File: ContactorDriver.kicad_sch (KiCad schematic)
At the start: 26 parts, among them Con1 LED, Con2 LED, J13 Conn_01x04, J14 Conn_01x04, Q2 IRLML0030, Q3 IRLML0030, U4 TCMT1106, U5 TCMT1106

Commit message: is it time to give up :3
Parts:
- renumbered C11 to C12, C12 to C13, C13 to C14, C14 to C15, D8 to D7, D9 to D8, J13 to J12, J14 to J13
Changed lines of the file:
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@@
 		(dnp no)
 		(fields_autoplaced yes)
-		(property "Reference" "#PWR053"
+		(property "Reference" "#PWR050"
 			(at 112.395 36.83 0)
 			(effects
@@
 			(project "VehicleControlUnit"
 				(path "/795c8e51-3ded-4d21-b864-aaff31c5def7/838dfc75-afcf-4845-8c43-fcef4e0ee00c"
-					(reference "#PWR053")
+					(reference "#PWR050")
 					(unit 1)
 				)
@@
 		(dnp no)
 		(fields_autoplaced yes)
-		(property "Reference" "C11"
+		(property "Reference" "C12"
 			(at 59.055 117.4749 0)
 			(effects
@@
 			(project ""
 				(path "/795c8e51-3ded-4d21-b864-aaff31c5def7/838dfc75-afcf-4845-8c43-fcef4e0ee00c"
-					(reference "C11")
+					(reference "C12")
 					(unit 1)
 				)
@@
 		(dnp no)
 		(fields_autoplaced yes)
-		(property "Reference" "C13"
+		(property "Reference" "C14"
 			(at 179.705 118.1099 0)
 			(effects
@@
 			(project "VehicleControlUnit"
 				(path "/795c8e51-3ded-4d21-b864-aaff31c5def7/838dfc75-afcf-4845-8c43-fcef4e0ee00c"
-					(reference "C13")
+					(reference "C14")
 					(unit 1)
 				)
@@
 		(dnp no)
 		(fields_autoplaced yes)
-		(property "Reference" "D8"
+		(property "Reference" "D7"
 			(at 114.935 43.8149 90)
 			(effects
@@
 			(project "VehicleControlUnit"
 				(path "/795c8e51-3ded-4d21-b864-aaff31c5def7/838dfc75-afcf-4845-8c43-fcef4e0ee00c"
-					(reference "D8")
+					(reference "D7")
 					(unit 1)
 				)
@@
 		(dnp no)
 		(fields_autoplaced yes)
-		(property "Reference" "#PWR054"
+		(property "Reference" "#PWR051"
 			(at 226.695 105.41 0)
 			(effects
@@
 			(project "VehicleControlUnit"
 				(path "/795c8e51-3ded-4d21-b864-aaff31c5def7/838dfc75-afcf-4845-8c43-fcef4e0ee00c"
-					(reference "#PWR054")
+					(reference "#PWR051")
 					(unit 1)
 				)
@@
 		(on_board yes)
 		(dnp no)
-		(property "Reference" "C12"
+		(property "Reference" "C13"
 			(at 100.965 112.3949 0)
 			(effects
@@
 			(project "VehicleControlUnit"
 				(path "/795c8e51-3ded-4d21-b864-aaff31c5def7/838dfc75-afcf-4845-8c43-fcef4e0ee00c"
-					(reference "C12")
+					(reference "C13")
 					(unit 1)
 				)
@@
 		(dnp no)
 		(fields_autoplaced yes)
-		(property "Reference" "#PWR055"
+		(property "Reference" "#PWR052"
 			(at 234.315 38.1 0)
 			(effects
@@
 			(project "VehicleControlUnit"
 				(path "/795c8e51-3ded-4d21-b864-aaff31c5def7/838dfc75-afcf-4845-8c43-fcef4e0ee00c"
-					(reference "#PWR055")
+					(reference "#PWR052")
 					(unit 1)
 				)
@@
 		(on_board yes)
 		(dnp no)
-		(property "Reference" "C14"
+		(property "Reference" "C15"
 			(at 222.885 113.0299 0)
 			(effects
@@
 			(project "VehicleControlUnit"
 				(path "/795c8e51-3ded-4d21-b864-aaff31c5def7/838dfc75-afcf-4845-8c43-fcef4e0ee00c"
-					(reference "C14")
+					(reference "C15")
 					(unit 1)
 				)
@@
 		(dnp no)
 		(fields_autoplaced yes)
-		(property "Reference" "#PWR052"
+		(property "Reference" "#PWR049"
 			(at 106.045 104.775 0)
 			(effects
@@
 			(project "VehicleControlUnit"
 				(path "/795c8e51-3ded-4d21-b864-aaff31c5def7/838dfc75-afcf-4845-8c43-fcef4e0ee00c"
-					(reference "#PWR052")
+					(reference "#PWR049")
 					(unit 1)
 				)
@@
 		(on_board yes)
 		(dnp no)
-		(property "Reference" "J14"
+		(property "Reference" "J13"
 			(at 245.745 106.6801 0)
 			(effects
@@
 			(project "VehicleControlUnit"
 				(path "/795c8e51-3ded-4d21-b864-aaff31c5def7/838dfc75-afcf-4845-8c43-fcef4e0ee00c"
-					(reference "J14")
+					(reference "J13")
 					(unit 1)
 				)
@@
 		(on_board yes)
 		(dnp no)
-		(property "Reference" "J13"
+		(property "Reference" "J12"
 			(at 123.825 106.0451 0)
 			(effects
@@
 			(project "VehicleControlUnit"
 				(path "/795c8e51-3ded-4d21-b864-aaff31c5def7/838dfc75-afcf-4845-8c43-fcef4e0ee00c"
-					(reference "J13")
+					(reference "J12")
 					(unit 1)
 				)
@@
 		(dnp no)
 		(fields_autoplaced yes)
-		(property "Reference" "D9"
+		(property "Reference" "D8"
 			(at 236.855 44.4499 90)
 			(effects
@@
 			(project "VehicleControlUnit"
 				(path "/795c8e51-3ded-4d21-b864-aaff31c5def7/838dfc75-afcf-4845-8c43-fcef4e0ee00c"
-					(reference "D9")
-					(unit 1)
-				)
+					(reference "D8")
+					(unit 1)
+				)

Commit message: 24v changes
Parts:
- R17, R19, R22, R24: value 2k -> 4k
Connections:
- net +12V renamed +24V
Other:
- note added: "MPre_Sense+"
- note added: "M_Sense+"

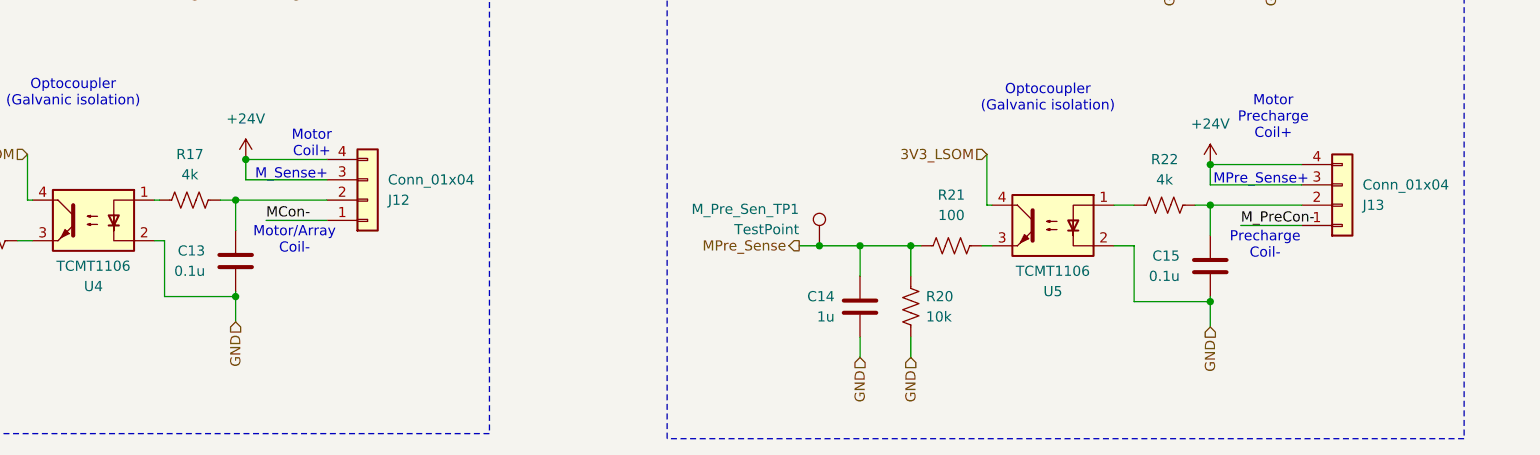
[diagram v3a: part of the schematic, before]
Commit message: moving to kicad-bild
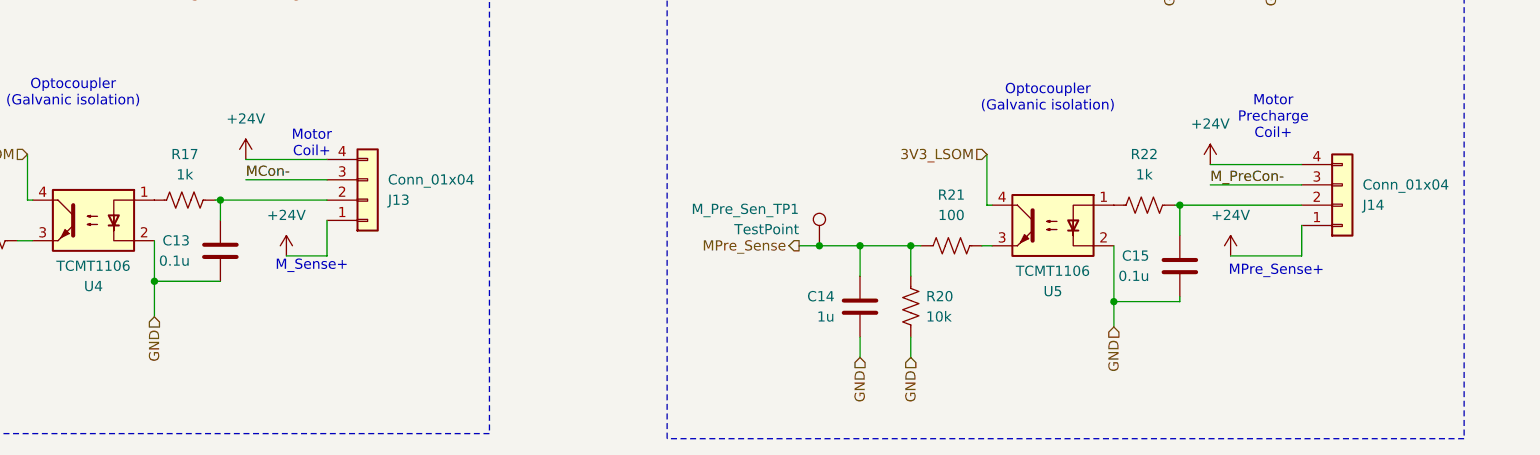
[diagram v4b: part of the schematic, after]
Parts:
- R17, R22: value 4k -> 1k
- renumbered J12 to J13, J13 to J14
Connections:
- net +24V: now also J13.1 (Pin_1), J14.1 (Pin_1); no longer J13.3 (Pin_3), J14.3 (Pin_3)
- net MCon-: now also J13.3 (Pin_3); no longer J13.1 (Pin_1)
- net M_PreCon-: now also J14.3 (Pin_3); no longer J14.1 (Pin_1)
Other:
- note removed: "Motor/Array Coil-"
- note removed: "Precharge Coil-"
- moved on the sheet: C13, C15, R17, R22

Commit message: fuck the rats nest im doing it tomorrow
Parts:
- D7, D8: footprint Active-PrechargeLib:SODFL4724X108N -> UTSVT_Passives:SODFL4724X108N
- J10: renamed from J13; footprint utsvt_conn:Molex_MicroFit3.0_1x4xP3.00mm_PolarizingPeg_Vertical -> UTSVT_Connectors:Molex_MicroFit3.0_1x4xP3.00mm_PolarizingPeg_Vertical
- J11: renamed from J14; footprint utsvt_conn:Molex_MicroFit3.0_1x4xP3.00mm_PolarizingPeg_Vertical -> UTSVT_Connectors:Molex_MicroFit3.0_1x4xP3.00mm_PolarizingPeg_Vertical
- renumbered C12 to C13, C13 to C14, C14 to C15, C15 to C16, R15 to R12, R16 to R13, R17 to R14, R18 to R15, R19 to R16, R20 to R17, R21 to R18, R22 to R19, R23 to R20, R24 to R21, U4 to U5, U5 to U6
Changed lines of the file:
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@@
 		(dnp no)
 		(fields_autoplaced yes)
-		(property "Reference" "R17"
+		(property "Reference" "R14"
 			(at 98.425 100.33 90)
 			(effects
@@
 			(project "VehicleControlUnit"
 				(path "/795c8e51-3ded-4d21-b864-aaff31c5def7/838dfc75-afcf-4845-8c43-fcef4e0ee00c"
-					(reference "R17")
+					(reference "R14")
 					(unit 1)
 				)
@@
 		(dnp no)
 		(fields_autoplaced yes)
-		(property "Reference" "#PWR054"
+		(property "Reference" "#PWR055"
 			(at 226.695 105.41 0)
 			(effects
@@
 			(project "VehicleControlUnit"
 				(path "/795c8e51-3ded-4d21-b864-aaff31c5def7/838dfc75-afcf-4845-8c43-fcef4e0ee00c"
-					(reference "#PWR054")
+					(reference "#PWR055")
 					(unit 1)
 				)
@@
 		(dnp no)
 		(fields_autoplaced yes)
-		(property "Reference" "R15"
+		(property "Reference" "R12"
 			(at 70.485 117.4749 0)
 			(effects
@@
 			(project ""
 				(path "/795c8e51-3ded-4d21-b864-aaff31c5def7/838dfc75-afcf-4845-8c43-fcef4e0ee00c"
-					(reference "R15")
+					(reference "R12")
 					(unit 1)
 				)
@@
 		(on_board yes)
 		(dnp no)
-		(property "Reference" "R18"
+		(property "Reference" "R15"
 			(at 102.235 69.2149 0)
 			(effects
@@
 			(project "VehicleControlUnit"
 				(path "/795c8e51-3ded-4d21-b864-aaff31c5def7/838dfc75-afcf-4845-8c43-fcef4e0ee00c"
-					(reference "R18")
+					(reference "R15")
 					(unit 1)
 				)
@@
 		(dnp no)
 		(fields_autoplaced yes)
-		(property "Reference" "U5"
+		(property "Reference" "U6"
 			(at 207.01 117.475 0)
 			(effects
@@
 			(project "VehicleControlUnit"
 				(path "/795c8e51-3ded-4d21-b864-aaff31c5def7/838dfc75-afcf-4845-8c43-fcef4e0ee00c"
-					(reference "U5")
+					(reference "U6")
 					(unit 1)
 				)
@@
 		(dnp no)
 		(fields_autoplaced yes)
-		(property "Reference" "C12"
+		(property "Reference" "C13"
 			(at 59.055 117.4749 0)
 			(effects
@@
 			(project ""
 				(path "/795c8e51-3ded-4d21-b864-aaff31c5def7/838dfc75-afcf-4845-8c43-fcef4e0ee00c"
-					(reference "C12")
+					(reference "C13")
 					(unit 1)
 				)
@@
 		(dnp no)
 		(fields_autoplaced yes)
-		(property "Reference" "R24"
+		(property "Reference" "R21"
 			(at 225.425 33.02 90)
 			(effects
@@
 			(project "VehicleControlUnit"
 				(path "/795c8e51-3ded-4d21-b864-aaff31c5def7/838dfc75-afcf-4845-8c43-fcef4e0ee00c"
-					(reference "R24")
+					(reference "R21")
 					(unit 1)
 				)
@@
 		(dnp no)
 		(fields_autoplaced yes)
-		(property "Reference" "R20"
+		(property "Reference" "R17"
 			(at 191.135 118.1099 0)
 			(effects
@@
 			(project "VehicleControlUnit"
 				(path "/795c8e51-3ded-4d21-b864-aaff31c5def7/838dfc75-afcf-4845-8c43-fcef4e0ee00c"
-					(reference "R20")
+					(reference "R17")
 					(unit 1)
 				)
@@
 		(dnp no)
 		(fields_autoplaced yes)
-		(property "Reference" "C14"
+		(property "Reference" "C15"
 			(at 179.705 118.1099 0)
 			(effects
@@
 			(project "VehicleControlUnit"
 				(path "/795c8e51-3ded-4d21-b864-aaff31c5def7/838dfc75-afcf-4845-8c43-fcef4e0ee00c"
-					(reference "C14")
+					(reference "C15")
 					(unit 1)
 				)
@@
 			)
 		)
-		(property "Footprint" "Active-PrechargeLib:SODFL4724X108N"
+		(property "Footprint" "UTSVT_Passives:SODFL4724X108N"
 			(at 112.395 45.085 0)
 			(effects
@@
 		(dnp no)
 		(fields_autoplaced yes)
-		(property "Reference" "R22"
+		(property "Reference" "R19"
 			(at 218.44 100.33 90)
 			(effects
@@
 			(project "VehicleControlUnit"
 				(path "/795c8e51-3ded-4d21-b864-aaff31c5def7/838dfc75-afcf-4845-8c43-fcef4e0ee00c"
-					(reference "R22")
+					(reference "R19")
 					(unit 1)
 				)
@@
 		(dnp no)
 		(fields_autoplaced yes)
-		(property "Reference" "#PWR053"
+		(property "Reference" "#PWR054"
 			(at 112.395 36.83 0)
 			(effects
@@
 			(project "VehicleControlUnit"
 				(path "/795c8e51-3ded-4d21-b864-aaff31c5def7/838dfc75-afcf-4845-8c43-fcef4e0ee00c"
-					(reference "#PWR053")
+					(reference "#PWR054")
 					(unit 1)
 				)
@@
 		(dnp no)
 		(fields_autoplaced yes)
-		(property "Reference" "#PWR051"
+		(property "Reference" "#PWR052"
 			(at 106.045 104.775 0)
 			(effects
@@
 			(project "VehicleControlUnit"
 				(path "/795c8e51-3ded-4d21-b864-aaff31c5def7/838dfc75-afcf-4845-8c43-fcef4e0ee00c"
-					(reference "#PWR051")
+					(reference "#PWR052")
 					(unit 1)
 				)
@@
 		(on_board yes)
 		(dnp no)
-		(property "Reference" "C13"
+		(property "Reference" "C14"
 			(at 99.06 111.1249 0)
 			(effects
@@
 			(project "VehicleControlUnit"
 				(path "/795c8e51-3ded-4d21-b864-aaff31c5def7/838dfc75-afcf-4845-8c43-fcef4e0ee00c"
-					(reference "C13")
+					(reference "C14")
 					(unit 1)
 				)
@@
 		(dnp no)
 		(fields_autoplaced yes)
-		(property "Reference" "#PWR052"
+		(property "Reference" "#PWR053"
 			(at 111.125 116.84 0)
 			(effects
@@
 			(project "VehicleControlUnit"
 				(path "/795c8e51-3ded-4d21-b864-aaff31c5def7/838dfc75-afcf-4845-8c43-fcef4e0ee00c"
-					(reference "#PWR052")
+					(reference "#PWR053")
 					(unit 1)
 				)
@@
 		(dnp no)
 		(fields_autoplaced yes)
-		(property "Reference" "R19"
+		(property "Reference" "R16"
 			(at 103.505 32.385 90)
 			(effects
@@
 			(project "VehicleControlUnit"
 				(path "/795c8e51-3ded-4d21-b864-aaff31c5def7/838dfc75-afcf-4845-8c43-fcef4e0ee00c"
-					(reference "R19")
+					(reference "R16")
 					(unit 1)
 				)
@@
 		(on_board yes)
 		(dnp no)
-		(property "Reference" "R23"
+		(property "Reference" "R20"
 			(at 224.155 69.8499 0)
 			(effects
@@
 			(project "VehicleControlUnit"
 				(path "/795c8e51-3ded-4d21-b864-aaff31c5def7/838dfc75-afcf-4845-8c43-fcef4e0ee00c"
-					(reference "R23")
+					(reference "R20")
 					(unit 1)
 				)
@@
 		(dnp no)
 		(fields_autoplaced yes)
-		(property "Reference" "R21"
+		(property "Reference" "R18"
 			(at 194.31 105.41 90)
 			(effects
@@
 			(project "VehicleControlUnit"
 				(path "/795c8e51-3ded-4d21-b864-aaff31c5def7/838dfc75-afcf-4845-8c43-fcef4e0ee00c"
-					(reference "R21")
+					(reference "R18")
 					(unit 1)
 				)
@@
 		(dnp no)
 		(fields_autoplaced yes)
-		(property "Reference" "#PWR056"
+		(property "Reference" "#PWR057"
 			(at 234.315 38.1 0)
 			(effects
@@
 			(project "VehicleControlUnit"
 				(path "/795c8e51-3ded-4d21-b864-aaff31c5def7/838dfc75-afcf-4845-8c43-fcef4e0ee00c"
-					(reference "#PWR056")
+					(reference "#PWR057")
 					(unit 1)
 				)
@@
 		(dnp no)
 		(fields_autoplaced yes)
-		(property "Reference" "#PWR055"
+		(property "Reference" "#PWR056"
 			(at 229.235 116.84 0)
 			(effects
@@
 			(project "VehicleControlUnit"
 				(path "/795c8e51-3ded-4d21-b864-aaff31c5def7/838dfc75-afcf-4845-8c43-fcef4e0ee00c"
-					(reference "#PWR055")
+					(reference "#PWR056")
 					(unit 1)
 				)
@@
 		(dnp no)
 		(fields_autoplaced yes)
-		(property "Reference" "R16"
+		(property "Reference" "R13"
 			(at 73.66 104.775 90)
 			(effects
@@
 			(project ""
 				(path "/795c8e51-3ded-4d21-b864-aaff31c5def7/838dfc75-afcf-4845-8c43-fcef4e0ee00c"
-					(reference "R16")
+					(reference "R13")
 					(unit 1)
 				)
@@
 		(on_board yes)
 		(dnp no)
-		(property "Reference" "C15"
+		(property "Reference" "C16"
 			(at 219.075 113.0299 0)
 			(effects
@@
 			(project "VehicleControlUnit"
 				(path "/795c8e51-3ded-4d21-b864-aaff31c5def7/838dfc75-afcf-4845-8c43-fcef4e0ee00c"
-					(reference "C15")
+					(reference "C16")
 					(unit 1)
 				)
@@
 		(on_board yes)
 		(dnp no)
-		(property "Reference" "J14"
+		(property "Reference" "J11"
 			(at 245.745 106.6801 0)
 			(effects
@@
 			)
 		)
-		(property "Footprint" "utsvt_conn:Molex_MicroFit3.0_1x4xP3.00mm_PolarizingPeg_Vertical"
+		(property "Footprint" "UTSVT_Connectors:Molex_MicroFit3.0_1x4xP3.00mm_PolarizingPeg_Vertical"
 			(at 243.205 106.68 0)
 			(effects
@@
 			(project "VehicleControlUnit"
 				(path "/795c8e51-3ded-4d21-b864-aaff31c5def7/838dfc75-afcf-4845-8c43-fcef4e0ee00c"
-					(reference "J14")
+					(reference "J11")
 					(unit 1)
 				)
@@
 		(on_board yes)
 		(dnp no)
-		(property "Reference" "J13"
+		(property "Reference" "J10"
 			(at 123.825 106.0451 0)
 			(effects
@@
 			)
 		)
-		(property "Footprint" "utsvt_conn:Molex_MicroFit3.0_1x4xP3.00mm_PolarizingPeg_Vertical"
+		(property "Footprint" "UTSVT_Connectors:Molex_MicroFit3.0_1x4xP3.00mm_PolarizingPeg_Vertical"
 			(at 121.285 106.045 0)
 			(effects
@@
 			(project "VehicleControlUnit"
 				(path "/795c8e51-3ded-4d21-b864-aaff31c5def7/838dfc75-afcf-4845-8c43-fcef4e0ee00c"
-					(reference "J13")
+					(reference "J10")
 					(unit 1)
 				)
@@
 		(dnp no)
 		(fields_autoplaced yes)
-		(property "Reference" "U4"
+		(property "Reference" "U5"
 			(at 86.995 116.84 0)
 			(effects
@@
 			(project "VehicleControlUnit"
 				(path "/795c8e51-3ded-4d21-b864-aaff31c5def7/838dfc75-afcf-4845-8c43-fcef4e0ee00c"
-					(reference "U4")
+					(reference "U5")
 					(unit 1)
 				)
@@
 			)
 		)
-		(property "Footprint" "Active-PrechargeLib:SODFL4724X108N"
+		(property "Footprint" "UTSVT_Passives:SODFL4724X108N"
 			(at 234.315 45.72 0)
 			(effects

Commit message: routing done
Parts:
- removed M_Pre_Sen_TP1, M_Sen_TP1: TestPoint, UTSVT_Special:TestPoint_HEX_3mmID, symbol Connector:TestPoint
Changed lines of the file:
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@@
-	)
-	(junction
-		(at 57.15 111.125)
-		(diameter 0)
-		(color 0 0 0 0)
 	)
 	(junction
@@
 	)
 	(junction
-		(at 177.8 111.76)
-		(diameter 0)
-		(color 0 0 0 0)
-	)
-	(junction
 		(at 99.695 64.135)
 		(diameter 0)
@@
 	(wire
 		(pts
-			(xy 177.8 111.76) (xy 182.88 111.76)
+			(xy 175.26 111.76) (xy 182.88 111.76)
 		)
 		(stroke
@@
 	(wire
 		(pts
-			(xy 57.15 111.125) (xy 62.23 111.125)
-		)
-		(stroke
-			(width 0)
-			(type default)
-		)
-	)
-	(wire
-		(pts
 			(xy 112.395 52.705) (xy 112.395 59.055)
 		)
@@
 	(wire
 		(pts
-			(xy 175.26 111.76) (xy 177.8 111.76)
-		)
-		(stroke
-			(width 0)
-			(type default)
-		)
-	)
-	(wire
-		(pts
 			(xy 116.205 103.505) (xy 106.045 103.505)
 		)
@@
 	(wire
 		(pts
-			(xy 57.15 111.125) (xy 54.61 111.125)
+			(xy 54.61 111.125) (xy 62.23 111.125)
 		)
 		(stroke
@@
 	)
 	(symbol
-		(lib_id "Connector:TestPoint")
-		(at 177.8 111.76 0)
-		(mirror y)
-		(unit 1)
-		(exclude_from_sim no)
-		(in_bom yes)
-		(on_board yes)
-		(dnp no)
-		(property "Reference" "M_Pre_Sen_TP1"
-			(at 175.26 107.1879 0)
-			(effects
-				(font
-					(size 1.27 1.27)
-				)
-				(justify left)
-			)
-		)
-		(property "Value" "TestPoint"
-			(at 175.26 109.7279 0)
-			(effects
-				(font
-					(size 1.27 1.27)
-				)
-				(justify left)
-			)
-		)
-		(property "Footprint" "UTSVT_Special:TestPoint_HEX_3mmID"
-			(at 172.72 111.76 0)
-			(effects
-				(font
-					(size 1.27 1.27)
-				)
-				(hide yes)
-			)
-		)
-		(property "Datasheet" "~"
-			(at 172.72 111.76 0)
-			(effects
-				(font
-					(size 1.27 1.27)
-				)
-				(hide yes)
-			)
-		)
-		(property "Description" "test point"
-			(at 177.8 111.76 0)
-			(effects
-				(font
-					(size 1.27 1.27)
-				)
-				(hide yes)
-			)
-		)
-		(pin "1"
-		)
-		(instances
-			(project "VehicleControlUnit"
-				(path "/795c8e51-3ded-4d21-b864-aaff31c5def7/838dfc75-afcf-4845-8c43-fcef4e0ee00c"
-					(reference "M_Pre_Sen_TP1")
-					(unit 1)
-				)
-			)
-		)
-	)
-	(symbol
 		(lib_id "power:+12V")
 		(at 106.045 100.965 0)
@@
 					(unit 1)
 				)
-			)
-		)
-	)
-	(symbol
-		(lib_id "Connector:TestPoint")
-		(at 57.15 111.125 0)
-		(mirror y)
-		(unit 1)
-		(exclude_from_sim no)
-		(in_bom yes)
-		(on_board yes)
-		(dnp no)
-		(property "Reference" "M_Sen_TP1"
-			(at 54.61 106.5529 0)
-			(effects
-				(font
-					(size 1.27 1.27)
-				)
-				(justify left)
-			)
-		)
-		(property "Value" "TestPoint"
-			(at 54.61 109.0929 0)
-			(effects
-				(font
-					(size 1.27 1.27)
-				)
-				(justify left)
-			)
-		)
-		(property "Footprint" "UTSVT_Special:TestPoint_HEX_3mmID"
-			(at 52.07 111.125 0)
-			(effects
-				(font
-					(size 1.27 1.27)
-				)
-				(hide yes)
-			)
-		)
-		(property "Datasheet" "~"
-			(at 52.07 111.125 0)
-			(effects
-				(font
-					(size 1.27 1.27)
-				)
-				(hide yes)
-			)
-		)
-		(property "Description" "test point"
-			(at 57.15 111.125 0)
-			(effects
-				(font
-					(size 1.27 1.27)
-				)
-				(hide yes)
-			)
-		)
-		(pin "1"
-		)
-		(instances
-			(project "VehicleControlUnit"
-				(path "/795c8e51-3ded-4d21-b864-aaff31c5def7/838dfc75-afcf-4845-8c43-fcef4e0ee00c"
-					(reference "M_Sen_TP1")
-					(unit 1)
-				)

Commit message: replace microfit with nanofit and some layout adjustments
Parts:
- J10, J11: footprint UTSVT_Connectors:Molex_MicroFit3.0_1x4xP3.00mm_PolarizingPeg_Vertical -> UTSVT_Connectors:Molex_Nano-Fit_105309-xx04_1x04_P2.50mm_Vertical
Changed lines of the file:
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@@
 			)
 		)
-		(property "Footprint" "UTSVT_Connectors:Molex_MicroFit3.0_1x4xP3.00mm_PolarizingPeg_Vertical"
+		(property "Footprint" "UTSVT_Connectors:Molex_Nano-Fit_105309-xx04_1x04_P2.50mm_Vertical"
 			(at 243.205 106.68 0)
 			(effects
@@
 			)
 		)
-		(property "Footprint" "UTSVT_Connectors:Molex_MicroFit3.0_1x4xP3.00mm_PolarizingPeg_Vertical"
+		(property "Footprint" "UTSVT_Connectors:Molex_Nano-Fit_105309-xx04_1x04_P2.50mm_Vertical"
 			(at 121.285 106.045 0)
 			(effects
